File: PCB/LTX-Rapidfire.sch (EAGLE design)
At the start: 51 parts, among them J1 F-1X08-SIP-100-40Y, Q1 2N3904, Q10 SS8550D, Q11 2N3906, Q12 2N3906, Q13 2N3904, Q2 2N3906, Q3 2N3904, Q4 2N3904, Q5 2N3904, Q6 2N3906, Q7 2N3906, Q8 2N3906, Q9 2N3904, SW1 F-1X02-SIP-100-40

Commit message: Labels and silkscreen!
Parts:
- renumbered SV1 to J2, U$1 to U2
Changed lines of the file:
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@@
 <grid distance="0.1" unitdist="inch" unit="inch" style="lines" multiple="1" display="no" altdistance="0.01" altunitdist="inch" altunit="inch"/>
 <layers>
-<layer number="1" name="Top" color="4" fill="1" visible="yes" active="no"/>
-<layer number="16" name="Bottom" color="1" fill="1" visible="yes" active="no"/>
-<layer number="17" name="Pads" color="2" fill="1" visible="yes" active="no"/>
-<layer number="18" name="Vias" color="2" fill="1" visible="yes" active="no"/>
-<layer number="19" name="Unrouted" color="6" fill="1" visible="yes" active="no"/>
-<layer number="20" name="Dimension" color="15" fill="1" visible="yes" active="no"/>
-<layer number="21" name="tPlace" color="7" fill="1" visible="yes" active="no"/>
-<layer number="22" name="bPlace" color="7" fill="1" visible="yes" active="no"/>
-<layer number="23" name="tOrigins" color="15" fill="1" visible="yes" active="no"/>
-<layer number="24" name="bOrigins" color="15" fill="1" visible="yes" active="no"/>
-<layer number="25" name="tNames" color="7" fill="1" visible="yes" active="no"/>
-<layer number="26" name="bNames" color="7" fill="1" visible="yes" active="no"/>
-<layer number="27" name="tValues" color="7" fill="1" visible="yes" active="no"/>
-<layer number="28" name="bValues" color="7" fill="1" visible="yes" active="no"/>
+<layer number="1" name="Top" color="4" fill="1" visible="no" active="no"/>
+<layer number="16" name="Bottom" color="1" fill="1" visible="no" active="no"/>
+<layer number="17" name="Pads" color="2" fill="1" visible="no" active="no"/>
+<layer number="18" name="Vias" color="2" fill="1" visible="no" active="no"/>
+<layer number="19" name="Unrouted" color="6" fill="1" visible="no" active="no"/>
+<layer number="20" name="Dimension" color="15" fill="1" visible="no" active="no"/>
+<layer number="21" name="tPlace" color="7" fill="1" visible="no" active="no"/>
+<layer number="22" name="bPlace" color="7" fill="1" visible="no" active="no"/>
+<layer number="23" name="tOrigins" color="15" fill="1" visible="no" active="no"/>
+<layer number="24" name="bOrigins" color="15" fill="1" visible="no" active="no"/>
+<layer number="25" name="tNames" color="7" fill="1" visible="no" active="no"/>
+<layer number="26" name="bNames" color="7" fill="1" visible="no" active="no"/>
+<layer number="27" name="tValues" color="7" fill="1" visible="no" active="no"/>
+<layer number="28" name="bValues" color="7" fill="1" visible="no" active="no"/>
 <layer number="29" name="tStop" color="7" fill="3" visible="no" active="no"/>
 <layer number="30" name="bStop" color="7" fill="6" visible="no" active="no"/>
@@
 <layer number="35" name="tGlue" color="7" fill="4" visible="no" active="no"/>
 <layer number="36" name="bGlue" color="7" fill="5" visible="no" active="no"/>
-<layer number="37" name="tTest" color="7" fill="1" visible="yes" active="no"/>
-<layer number="38" name="bTest" color="7" fill="1" visible="yes" active="no"/>
+<layer number="37" name="tTest" color="7" fill="1" visible="no" active="no"/>
+<layer number="38" name="bTest" color="7" fill="1" visible="no" active="no"/>
 <layer number="39" name="tKeepout" color="4" fill="11" visible="no" active="no"/>
 <layer number="40" name="bKeepout" color="1" fill="11" visible="no" active="no"/>
@@
 <layer number="44" name="Drills" color="7" fill="1" visible="no" active="no"/>
 <layer number="45" name="Holes" color="7" fill="1" visible="no" active="no"/>
-<layer number="46" name="Milling" color="3" fill="1" visible="yes" active="no"/>
-<layer number="47" name="Measures" color="7" fill="1" visible="yes" active="no"/>
-<layer number="48" name="Document" color="7" fill="1" visible="yes" active="no"/>
-<layer number="49" name="Reference" color="7" fill="1" visible="yes" active="no"/>
-<layer number="50" name="dxf" color="7" fill="1" visible="yes" active="no"/>
-<layer number="51" name="tDocu" color="7" fill="1" visible="yes" active="no"/>
-<layer number="52" name="bDocu" color="7" fill="1" visible="yes" active="no"/>
-<layer number="53" name="tGND_GNDA" color="7" fill="9" visible="yes" active="no"/>
-<layer number="54" name="bGND_GNDA" color="1" fill="9" visible="yes" active="no"/>
-<layer number="56" name="wert" color="7" fill="1" visible="yes" active="no"/>
+<layer number="46" name="Milling" color="3" fill="1" visible="no" active="no"/>
+<layer number="47" name="Measures" color="7" fill="1" visible="no" active="no"/>
+<layer number="48" name="Document" color="7" fill="1" visible="no" active="no"/>
+<layer number="49" name="Reference" color="7" fill="1" visible="no" active="no"/>
+<layer number="50" name="dxf" color="7" fill="1" visible="no" active="no"/>
+<layer number="51" name="tDocu" color="7" fill="1" visible="no" active="no"/>
+<layer number="52" name="bDocu" color="7" fill="1" visible="no" active="no"/>
+<layer number="53" name="tGND_GNDA" color="7" fill="9" visible="no" active="no"/>
+<layer number="54" name="bGND_GNDA" color="1" fill="9" visible="no" active="no"/>
+<layer number="56" name="wert" color="7" fill="1" visible="no" active="no"/>
 <layer number="91" name="Nets" color="2" fill="1" visible="yes" active="yes"/>
 <layer number="92" name="Busses" color="1" fill="1" visible="yes" active="yes"/>
@@
 <part name="SW1" library="con-headers-jp" deviceset="F-1X02-" device="SIP-100-40"/>
 <part name="C3" library="rcl" deviceset="C-EU" device="025-025X050" value="0.1uF"/>
-<part name="U$1" library="izzy" deviceset="Z8F082A" device="DIL-8"/>
-<part name="SV1" library="izzy" deviceset="MA03-2" device=""/>
+<part name="U2" library="izzy" deviceset="Z8F082A" device="DIL-8"/>
+<part name="J2" library="izzy" deviceset="MA03-2" device=""/>
 <part name="R26" library="rcl" deviceset="R-US_" device="0204/2V" value="10k"/>
 <part name="R21" library="rcl" deviceset="R-US_" device="0204/7" value="200k"/>
@@
 <instance part="SW1" gate="G$1" x="50.8" y="40.64" rot="R180"/>
 <instance part="C3" gate="G$1" x="137.16" y="68.58" rot="R180"/>
-<instance part="U$1" gate="G$1" x="175.26" y="81.28"/>
-<instance part="SV1" gate="1" x="142.24" y="45.72"/>
+<instance part="U2" gate="G$1" x="175.26" y="81.28"/>
+<instance part="J2" gate="1" x="142.24" y="45.72"/>
 <instance part="R26" gate="G$1" x="142.24" y="35.56" rot="R180"/>
 <instance part="R21" gate="G$1" x="88.9" y="50.8" rot="R270"/>
@@
 </segment>
 <segment>
-<pinref part="U$1" gate="G$1" pin="VSS"/>
+<pinref part="U2" gate="G$1" pin="VSS"/>
 <wire x1="152.4" y1="71.12" x2="149.86" y2="71.12" width="0.1524" layer="91"/>
 <label x="149.86" y="71.12" size="1.778" layer="95" rot="R180"/>
 </segment>
 <segment>
-<pinref part="SV1" gate="1" pin="3"/>
+<pinref part="J2" gate="1" pin="3"/>
 <wire x1="149.86" y1="45.72" x2="152.4" y2="45.72" width="0.1524" layer="91"/>
-<pinref part="SV1" gate="1" pin="5"/>
+<pinref part="J2" gate="1" pin="5"/>
 <wire x1="149.86" y1="48.26" x2="152.4" y2="48.26" width="0.1524" layer="91"/>
 <wire x1="152.4" y1="48.26" x2="152.4" y2="45.72" width="0.1524" layer="91"/>
@@
 <label x="137.16" y="76.2" size="1.778" layer="95" rot="R90"/>
 <junction x="137.16" y="73.66"/>
-<pinref part="U$1" gate="G$1" pin="VDD"/>
+<pinref part="U2" gate="G$1" pin="VDD"/>
 <wire x1="137.16" y1="73.66" x2="152.4" y2="73.66" width="0.1524" layer="91"/>
 </segment>
 <segment>
-<pinref part="SV1" gate="1" pin="1"/>
+<pinref part="J2" gate="1" pin="1"/>
 <wire x1="149.86" y1="43.18" x2="152.4" y2="43.18" width="0.1524" layer="91"/>
 <wire x1="152.4" y1="43.18" x2="154.94" y2="43.18" width="0.1524" layer="91"/>
@@
 </segment>
 <segment>
-<pinref part="U$1" gate="G$1" pin="PA1/T0OUT/XOUT/ANA3/VREF/CLKIN"/>
+<pinref part="U2" gate="G$1" pin="PA1/T0OUT/XOUT/ANA3/VREF/CLKIN"/>
 <wire x1="152.4" y1="88.9" x2="149.86" y2="88.9" width="0.1524" layer="91"/>
 <label x="149.86" y="88.9" size="1.778" layer="95" rot="R180"/>
@@
 </segment>
 <segment>
-<pinref part="U$1" gate="G$1" pin="PA3/!CTS0!/ANA2/COUT/AMPINP/T1IN"/>
+<pinref part="U2" gate="G$1" pin="PA3/!CTS0!/ANA2/COUT/AMPINP/T1IN"/>
 <wire x1="152.4" y1="83.82" x2="149.86" y2="83.82" width="0.1524" layer="91"/>
 <label x="149.86" y="83.82" size="1.778" layer="95" rot="R180"/>
@@
 </segment>
 <segment>
-<pinref part="U$1" gate="G$1" pin="PA4/RXD0/ANA1/CINN/AMPINN"/>
+<pinref part="U2" gate="G$1" pin="PA4/RXD0/ANA1/CINN/AMPINN"/>
 <wire x1="152.4" y1="81.28" x2="149.86" y2="81.28" width="0.1524" layer="91"/>
 <label x="149.86" y="81.28" size="1.778" layer="95" rot="R180"/>
@@
 </segment>
 <segment>
-<pinref part="U$1" gate="G$1" pin="PA5/TXD0/!T1OUT!/ANA0/CINP/AMPOUT"/>
+<pinref part="U2" gate="G$1" pin="PA5/TXD0/!T1OUT!/ANA0/CINP/AMPOUT"/>
 <wire x1="152.4" y1="78.74" x2="149.86" y2="78.74" width="0.1524" layer="91"/>
 <label x="149.86" y="78.74" size="1.778" layer="95" rot="R180"/>
@@
 </segment>
 <segment>
-<pinref part="U$1" gate="G$1" pin="PA2/!RESET!/DE0/TIOUT"/>
+<pinref part="U2" gate="G$1" pin="PA2/!RESET!/DE0/TIOUT"/>
 <wire x1="152.4" y1="86.36" x2="149.86" y2="86.36" width="0.1524" layer="91"/>
 <label x="149.86" y="86.36" size="1.778" layer="95" rot="R180"/>
 </segment>
 <segment>
-<pinref part="SV1" gate="1" pin="2"/>
+<pinref part="J2" gate="1" pin="2"/>
 <wire x1="134.62" y1="43.18" x2="132.08" y2="43.18" width="0.1524" layer="91"/>
 <wire x1="129.54" y1="43.18" x2="132.08" y2="43.18" width="0.1524" layer="91"/>
@@
 </segment>
 <segment>
-<pinref part="U$1" gate="G$1" pin="PA0/T0IN/!T0OUT!/XIN/DBG"/>
+<pinref part="U2" gate="G$1" pin="PA0/T0IN/!T0OUT!/XIN/DBG"/>
 <wire x1="152.4" y1="91.44" x2="149.86" y2="91.44" width="0.1524" layer="91"/>
 <label x="149.86" y="91.44" size="1.778" layer="95" rot="R180"/>
 </segment>
 <segment>
-<pinref part="SV1" gate="1" pin="4"/>
+<pinref part="J2" gate="1" pin="4"/>
 <wire x1="134.62" y1="45.72" x2="129.54" y2="45.72" width="0.1524" layer="91"/>
 <label x="129.54" y="45.72" size="1.778" layer="95" rot="R180"/>

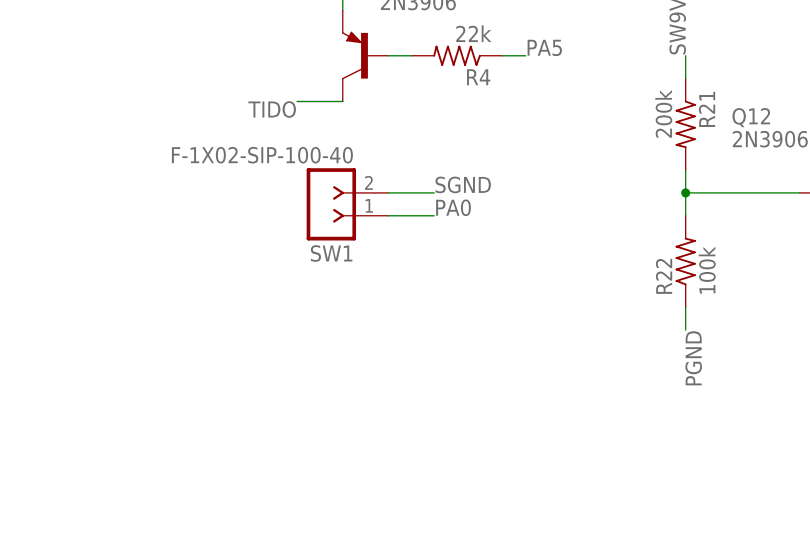
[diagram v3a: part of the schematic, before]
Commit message: A resistor got missed! Whoops. Put that back in...
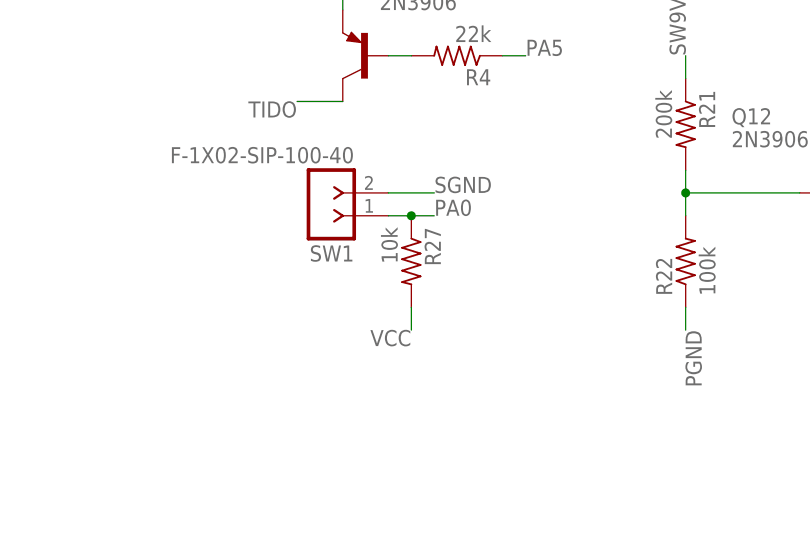
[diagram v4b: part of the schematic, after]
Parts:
- added R27: 10k, rcl:R-US_0204/2V
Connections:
- net PA0: now also R27.1
- net VCC: now also R27.2
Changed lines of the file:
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@@
 <part name="R23" library="rcl" deviceset="R-US_" device="0204/7" value="1k"/>
 <part name="Q12" library="transistor-pnp" deviceset="2N3906" device=""/>
+<part name="R27" library="rcl" deviceset="R-US_" device="0204/2V" value="10k"/>
 </parts>
 <sheets>
@@
 <instance part="R23" gate="G$1" x="106.68" y="30.48" rot="R270"/>
 <instance part="Q12" gate="G$1" x="104.14" y="43.18"/>
+<instance part="R27" gate="G$1" x="58.42" y="35.56" rot="R270"/>
 </instances>
 <busses>
@@
 <wire x1="106.68" y1="48.26" x2="106.68" y2="58.42" width="0.1524" layer="91"/>
 <label x="106.68" y="58.42" size="1.778" layer="95" rot="R90"/>
+</segment>
+<segment>
+<pinref part="R27" gate="G$1" pin="2"/>
+<wire x1="58.42" y1="30.48" x2="58.42" y2="27.94" width="0.1524" layer="91"/>
+<label x="58.42" y="27.94" size="1.778" layer="95" rot="R180"/>
 </segment>
 </net>
@@
 <segment>
 <pinref part="SW1" gate="G$1" pin="1"/>
-<wire x1="55.88" y1="40.64" x2="60.96" y2="40.64" width="0.1524" layer="91"/>
+<wire x1="55.88" y1="40.64" x2="58.42" y2="40.64" width="0.1524" layer="91"/>
 <label x="60.96" y="40.64" size="1.778" layer="95"/>
-</segment>
-<segment>
+<pinref part="R27" gate="G$1" pin="1"/>
+<wire x1="58.42" y1="40.64" x2="60.96" y2="40.64" width="0.1524" layer="91"/>
+<junction x="58.42" y="40.64"/>
+</segment>
+<segment>

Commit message: Replace R19 out so you can fit a 1/2W resistor in.
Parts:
- R19: device rcl:R-US_0204/7 -> rcl:R-US_0207/10
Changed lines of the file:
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@@
 <layers>
 <layer number="1" name="Top" color="4" fill="1" visible="no" active="no"/>
+<layer number="2" name="Route2" color="1" fill="3" visible="no" active="no"/>
+<layer number="3" name="Route3" color="4" fill="3" visible="no" active="no"/>
+<layer number="4" name="Route4" color="1" fill="4" visible="no" active="no"/>
+<layer number="5" name="Route5" color="4" fill="4" visible="no" active="no"/>
+<layer number="6" name="Route6" color="1" fill="8" visible="no" active="no"/>
+<layer number="7" name="Route7" color="4" fill="8" visible="no" active="no"/>
+<layer number="8" name="Route8" color="1" fill="2" visible="no" active="no"/>
+<layer number="9" name="Route9" color="4" fill="2" visible="no" active="no"/>
+<layer number="10" name="Route10" color="1" fill="7" visible="no" active="no"/>
+<layer number="11" name="Route11" color="4" fill="7" visible="no" active="no"/>
+<layer number="12" name="Route12" color="1" fill="5" visible="no" active="no"/>
+<layer number="13" name="Route13" color="4" fill="5" visible="no" active="no"/>
+<layer number="14" name="Route14" color="1" fill="6" visible="no" active="no"/>
+<layer number="15" name="Route15" color="4" fill="6" visible="no" active="no"/>
 <layer number="16" name="Bottom" color="1" fill="1" visible="no" active="no"/>
 <layer number="17" name="Pads" color="2" fill="1" visible="no" active="no"/>
@@
 <part name="R18" library="rcl" deviceset="R-US_" device="0204/2V" value="1k"/>
 <part name="D2" library="led" deviceset="LED" device="5MM"/>
-<part name="R19" library="rcl" deviceset="R-US_" device="0204/7" value="3.9"/>
+<part name="R19" library="rcl" deviceset="R-US_" device="0207/10" value="3.9"/>
 <part name="R13" library="rcl" deviceset="R-US_" device="0204/2V" value="1.3k"/>
 <part name="R12" library="rcl" deviceset="R-US_" device="0204/7" value="3.3k"/>
